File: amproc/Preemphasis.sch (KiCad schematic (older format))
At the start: 29 parts, among them Q2 BC546, Q3 BC546, Q4 BC556, U3 TL072, U4 LM13700, U5 TL072, U6 TL072

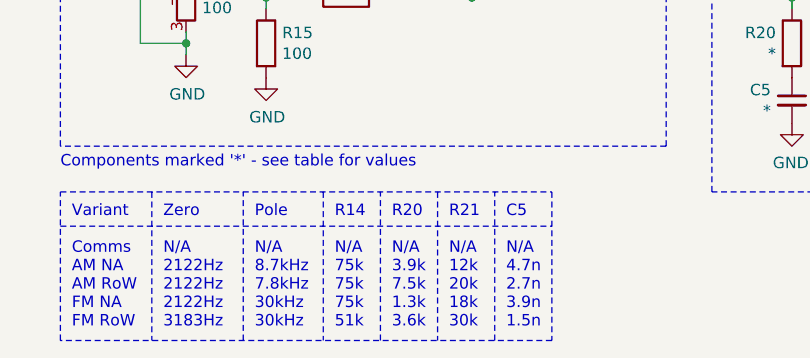
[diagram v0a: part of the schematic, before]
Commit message: Changed LPF, pre-emphasis component values in AM (NA and RoW) variants to correct bandwidth
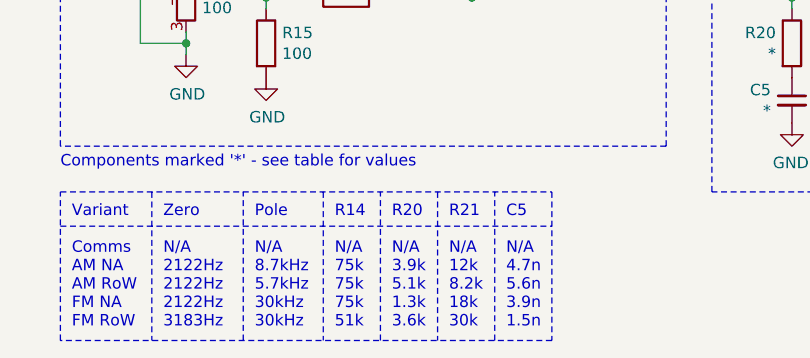
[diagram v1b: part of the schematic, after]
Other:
- note added: "C5\n\nN/A\n4.7n\n5.6n\n3.9n\n1.5n"
- note added: "Pole\n\nN/A\n8.7kHz\n5.7kHz\n30kHz\n30kHz"
- note added: "R20\n\nN/A\n3.9k\n5.1k\n1.3k\n3.6k"
- note added: "R21\n\nN/A\n12k\n8.2k\n18k\n30k"
- note removed: "C5\n\nN/A\n4.7n\n2.7n\n3.9n\n1.5n"
- note removed: "Pole\n\nN/A\n8.7kHz\n7.8kHz\n30kHz\n30kHz"
- note removed: "R20\n\nN/A\n3.9k\n7.5k\n1.3k\n3.6k"
- note removed: "R21\n\nN/A\n12k\n20k\n18k\n30k"
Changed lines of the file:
@@
 Zero\n\nN/A\n2122Hz\n2122Hz\n2122Hz\n3183Hz
 Text Notes 3450 6450 0    50   ~ 0
-Pole\n\nN/A\n8.7kHz\n7.8kHz\n30kHz\n30kHz
+Pole\n\nN/A\n8.7kHz\n5.7kHz\n30kHz\n30kHz
 Text Notes 3800 6450 0    50   ~ 0
 R14\n\nN/A\n75k\n75k\n75k\n51k
 Text Notes 4050 6450 0    50   ~ 0
-R20\n\nN/A\n3.9k\n7.5k\n1.3k\n3.6k
+R20\n\nN/A\n3.9k\n5.1k\n1.3k\n3.6k
 Text Notes 4300 6450 0    50   ~ 0
-R21\n\nN/A\n12k\n20k\n18k\n30k
+R21\n\nN/A\n12k\n8.2k\n18k\n30k
 Wire Notes Line style solid
 	3000 5850 3000 6500
@@
 	4500 6500 4500 5850
 Text Notes 4550 6450 0    50   ~ 0
-C5\n\nN/A\n4.7n\n2.7n\n3.9n\n1.5n
+C5\n\nN/A\n4.7n\n5.6n\n3.9n\n1.5n
 Wire Notes Line style solid
 	2600 5850 4750 5850

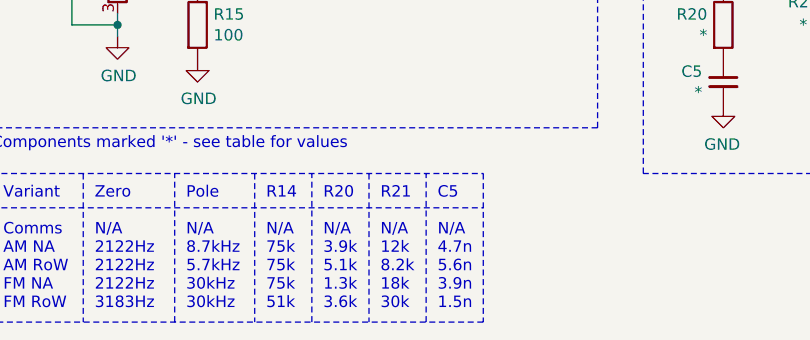
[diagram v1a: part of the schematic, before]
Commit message: Optimise pre-emphasis network values
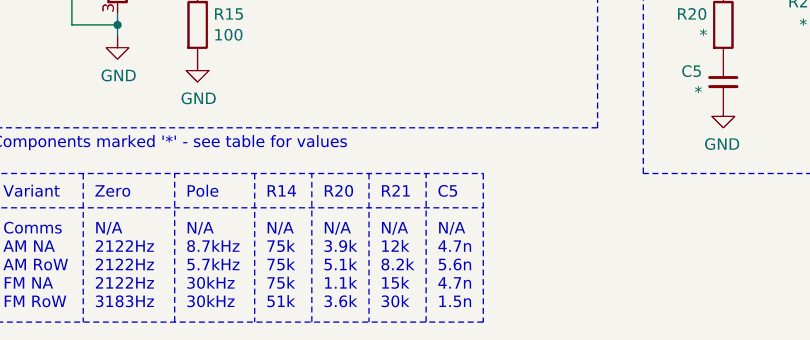
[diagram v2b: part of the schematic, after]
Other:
- note added: "C5\n\nN/A\n4.7n\n5.6n\n4.7n\n1.5n"
- note added: "R20\n\nN/A\n3.9k\n5.1k\n1.1k\n3.6k"
- note added: "R21\n\nN/A\n12k\n8.2k\n15k\n30k"
- note removed: "C5\n\nN/A\n4.7n\n5.6n\n3.9n\n1.5n"
- note removed: "R20\n\nN/A\n3.9k\n5.1k\n1.3k\n3.6k"
- note removed: "R21\n\nN/A\n12k\n8.2k\n18k\n30k"
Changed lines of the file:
@@
 Text Notes 3800 6450 0    50   ~ 0
 R14\n\nN/A\n75k\n75k\n75k\n51k
-Text Notes 4050 6450 0    50   ~ 0
-R20\n\nN/A\n3.9k\n5.1k\n1.3k\n3.6k
-Text Notes 4300 6450 0    50   ~ 0
-R21\n\nN/A\n12k\n8.2k\n18k\n30k
 Wire Notes Line style solid
 	3000 5850 3000 6500
@@
 Wire Notes Line style solid
 	4500 6500 4500 5850
-Text Notes 4550 6450 0    50   ~ 0
-C5\n\nN/A\n4.7n\n5.6n\n3.9n\n1.5n
 Wire Notes Line style solid
 	2600 5850 4750 5850
@@
 	3150 5200 3150 5250
 Connection ~ 3150 5200
+Text Notes 4550 6450 0    50   ~ 0
+C5\n\nN/A\n4.7n\n5.6n\n4.7n\n1.5n
+Text Notes 4300 6450 0    50   ~ 0
+R21\n\nN/A\n12k\n8.2k\n15k\n30k
+Text Notes 4050 6450 0    50   ~ 0
+R20\n\nN/A\n3.9k\n5.1k\n1.1k\n3.6k
 $EndSCHEMATC
